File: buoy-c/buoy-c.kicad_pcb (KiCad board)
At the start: 4 copper layers, 49.3 x 87 mm, 102 parts, among them J1 UJ31-CH-G2-SMT-TR, J10 Conn_01x10_Male, J11 TERM-BLK-2P, J12 TERM-BLK-2P, J13 Conn_01x05_Male, J2 BAT-HLD-001-THM, J3 TERM-BLK-2P, J4 U.FL-R-SMT-1_10_, J5 BH-18650-PC, J6 Conn_01x03_Male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

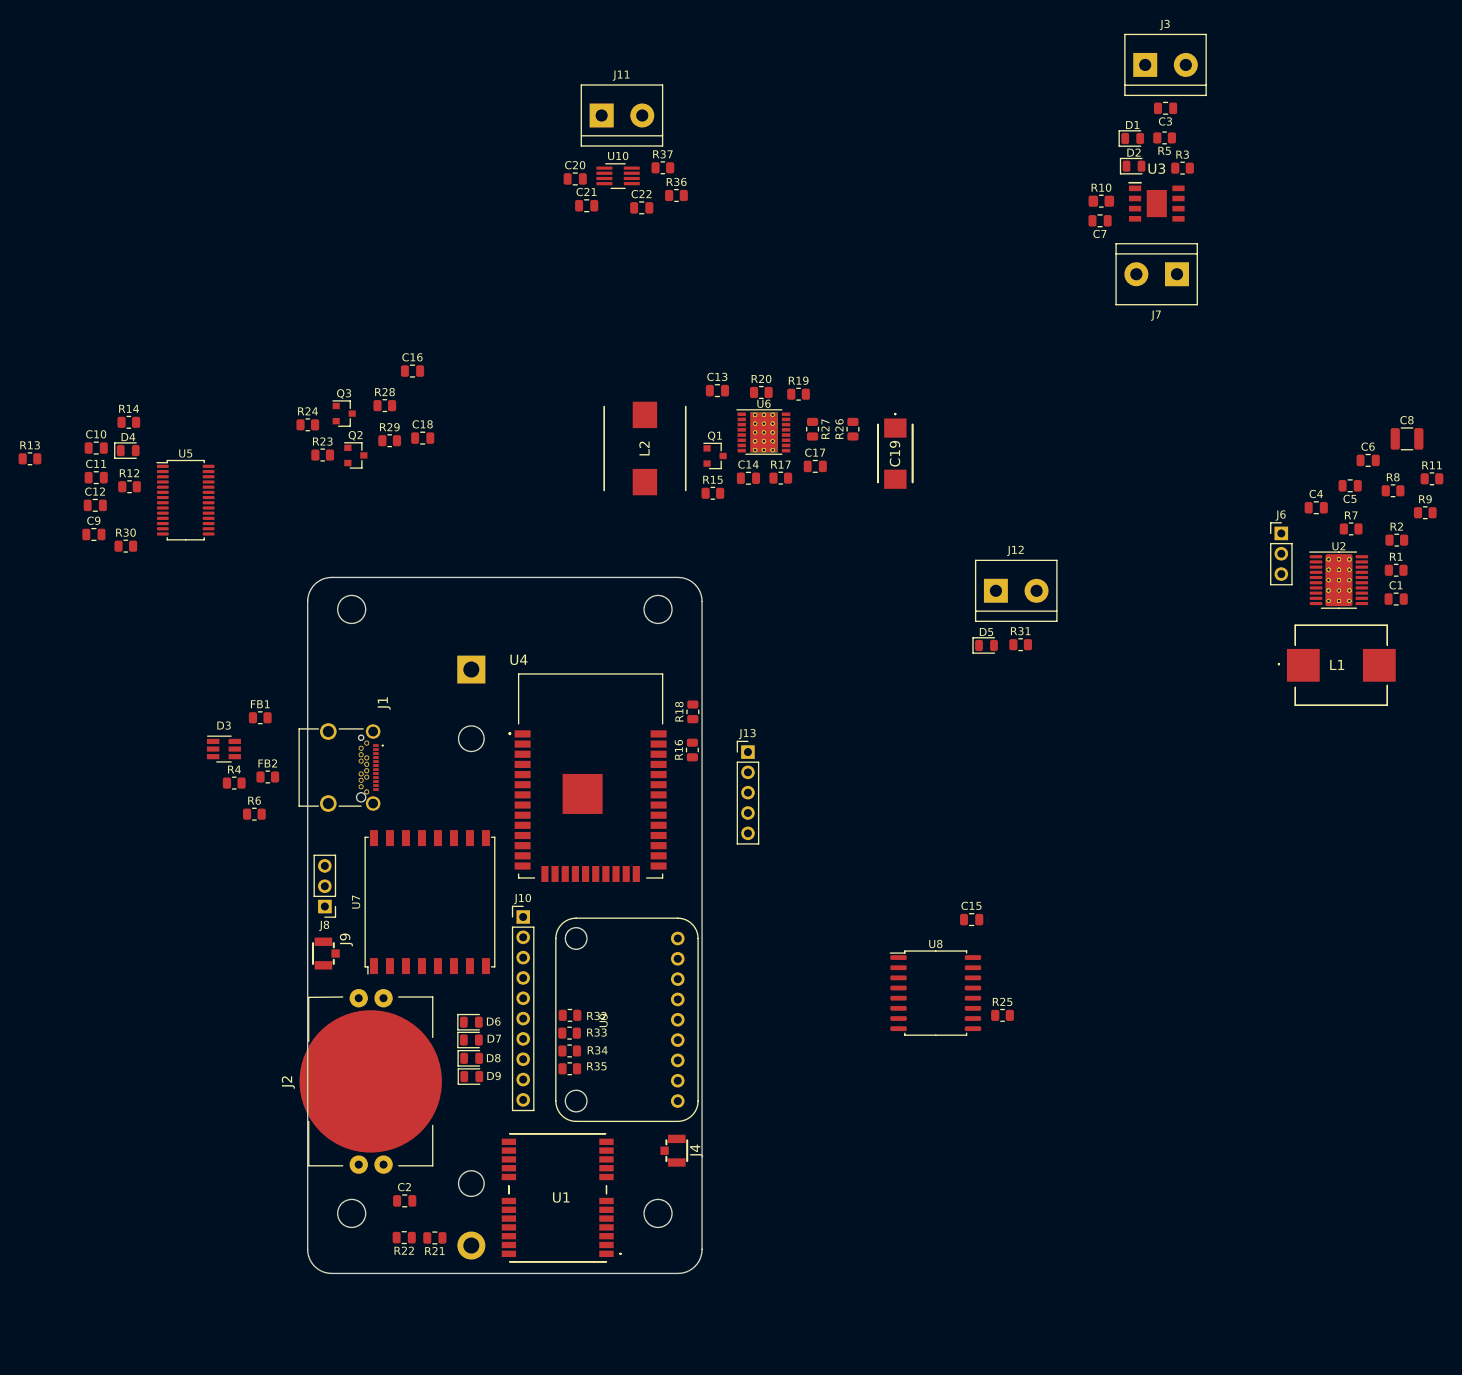
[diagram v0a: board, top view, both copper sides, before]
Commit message: Placed components in the PCB
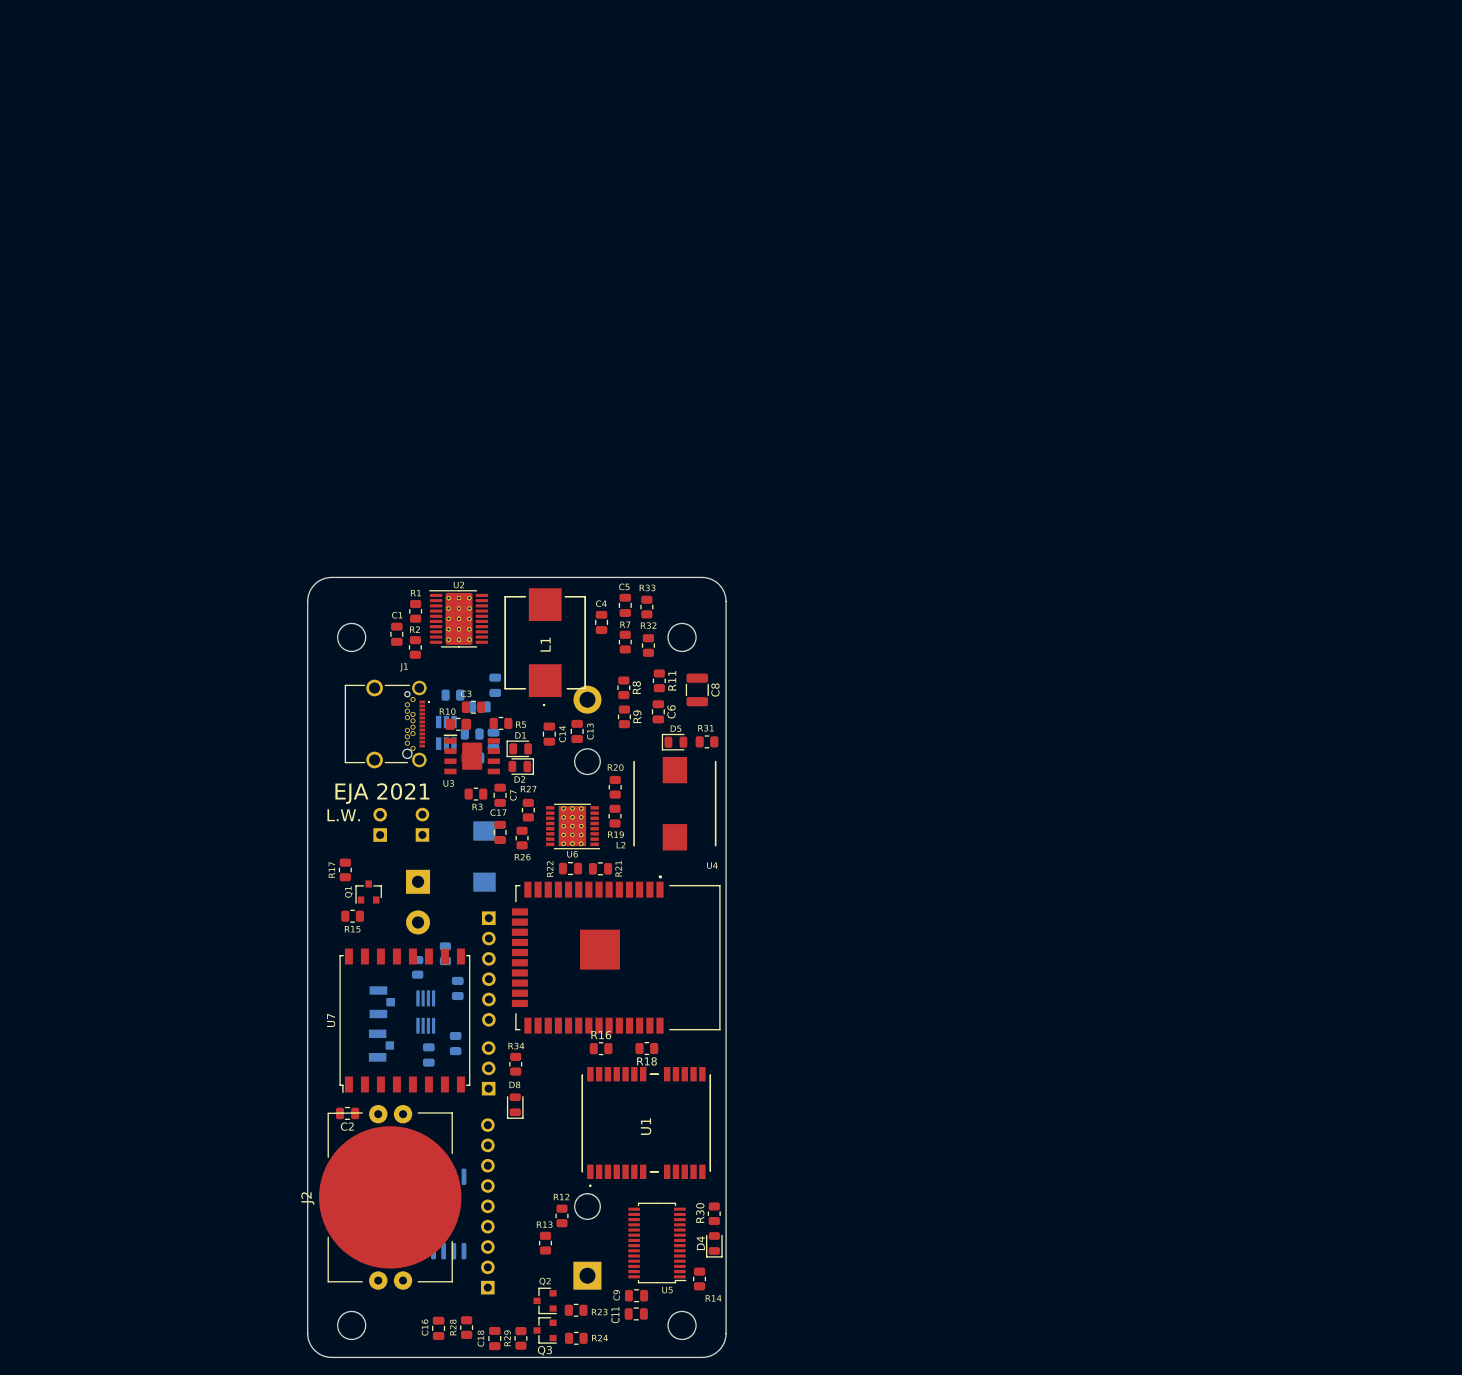
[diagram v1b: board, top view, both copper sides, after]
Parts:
- removed D6: GREEN-CLEAR, LED_SMD:LED_0805_2012Metric
- removed D7: ORANGE-CLEAR, LED_SMD:LED_0805_2012Metric
- removed D9: RED-CLEAR, LED_SMD:LED_0805_2012Metric
- removed J12: TERM-BLK-2P, TerminalBlock:TerminalBlock_bornier-2_P5.08mm
- removed J13: Conn_01x05_Male, Connector_PinHeader_2.54mm:PinHeader_1x05_P2.54mm_Vertical
- removed J6: Conn_01x03_Male, Connector_PinHeader_2.54mm:PinHeader_1x03_P2.54mm_Vertical
- removed R35: 620, Resistor_SMD:R_0805_2012Metric
- removed U9: ADXL343-EVAL, ADXL343-EVAL:ADXL343-EVAL
- added J14: Conn_01x09_Male, Connector_PinHeader_2.54mm:PinHeader_1x09_P2.54mm_Vertical, B.Cu at (122.5, 188.8)
- C10, C12, C15, C19, C20, C21, C22, D3, FB1, FB2, J11, J4, J8, J9, R25, R36, R37, R4, R6, U10, U8: moved to B.Cu
- J10: value Conn_01x10_Male -> Conn_01x06_Male; footprint Connector_PinHeader_2.54mm:PinHeader_1x10_P2.54mm_Vertical -> Connector_PinHeader_2.54mm:PinHeader_1x06_P2.54mm_Vertical; moved to B.Cu
- J3, J7: value TERM-BLK-2P -> Conn_01x02_Male; footprint TerminalBlock:TerminalBlock_bornier-2_P5.08mm -> Connector_PinHeader_2.54mm:PinHeader_1x02_P2.54mm_Vertical; moved to B.Cu
- R32, R33: value 620 -> 0
- moved J3 132.0 mm to (114.3, 132.2)
- moved R14 128.7 mm to (149.0, 187.7), turned to 90 degrees
- moved C1 125.0 mm to (111.1, 107.1), turned to 270 degrees
- moved C11 124.4 mm to (141.1, 192.1)
- moved R2 123.4 mm to (113.5, 108.8), turned to 270 degrees
- moved D4 123.2 mm to (150.8, 183.3), turned to 90 degrees
- moved R1 122.7 mm to (113.5, 104.2), turned to 90 degrees
- moved J7 121.8 mm to (109.1, 132.2), turned to 0 degrees
- moved C16 119.7 mm to (116.4, 193.9), turned to 270 degrees
- moved R24 119.0 mm to (133.6, 195.1)
- moved R3 118.0 mm to (121.0, 127.1)
- moved Q3 117.3 mm to (129.7, 194.1), turned to 180 degrees
- moved R13 117.3 mm to (129.7, 183.2), turned to 90 degrees
- moved C9 116.9 mm to (141.1, 189.8)
- moved R28 115.7 mm to (119.9, 193.8), turned to 90 degrees
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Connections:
- net Net-(D3-Pad3) renamed /FB1
- net Net-(D3-Pad4) renamed /FB2
- J10 pad 2: ESP_IO13 -> ESP_IO6
- J10 pad 3: ESP_IO9 -> ESP_IO7
- J10 pad 4: ESP_IO10 -> ESP_IO8
- J10 pad 5: ESP_IO11 -> ESP_IO15
- J10 pad 6: ESP_IO6 -> ESP_IO2
- R16 pad 1: +BATT -> VDD
- R18 pad 1: +BATT -> VDD
- R32 pad 1: ESP_IO13 -> VDD
- R32 pad 2: Net-(D6-Pad2) -> +3V3
- R33 pad 1: ESP_IO6 -> +BATT
- R33 pad 2: Net-(D7-Pad2) -> VDD
- R34 pad 1: ESP_IO7 -> ESP_IO2
- U4 pad 14: ESP_IO12 -> Net-(U4-Pad14)
- U4 pad 16: ESP_IO13 -> Net-(U4-Pad16)
- U4 pad 17: ESP_IO9 -> Net-(U4-Pad17)
- U4 pad 18: ESP_IO10 -> Net-(U4-Pad18)
- U4 pad 19: ESP_IO11 -> Net-(U4-Pad19)
- U4 pad 4: ESP_IO36 -> Net-(U4-Pad4)
- U4 pad 5: ESP_IO39 -> Net-(U4-Pad5)
- U4 pad 7: ESP_IO35 -> Net-(U4-Pad7)
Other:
- board size 49.3 x 87 mm -> 52.3 x 97.5 mm
- board text added: "+"
- board text added: "-"
- board text added: "5V"
- board text added: "BATT"
- board text added: "EJA 2021"
- board text added: "L.W."
- board text added: "SWITCH"

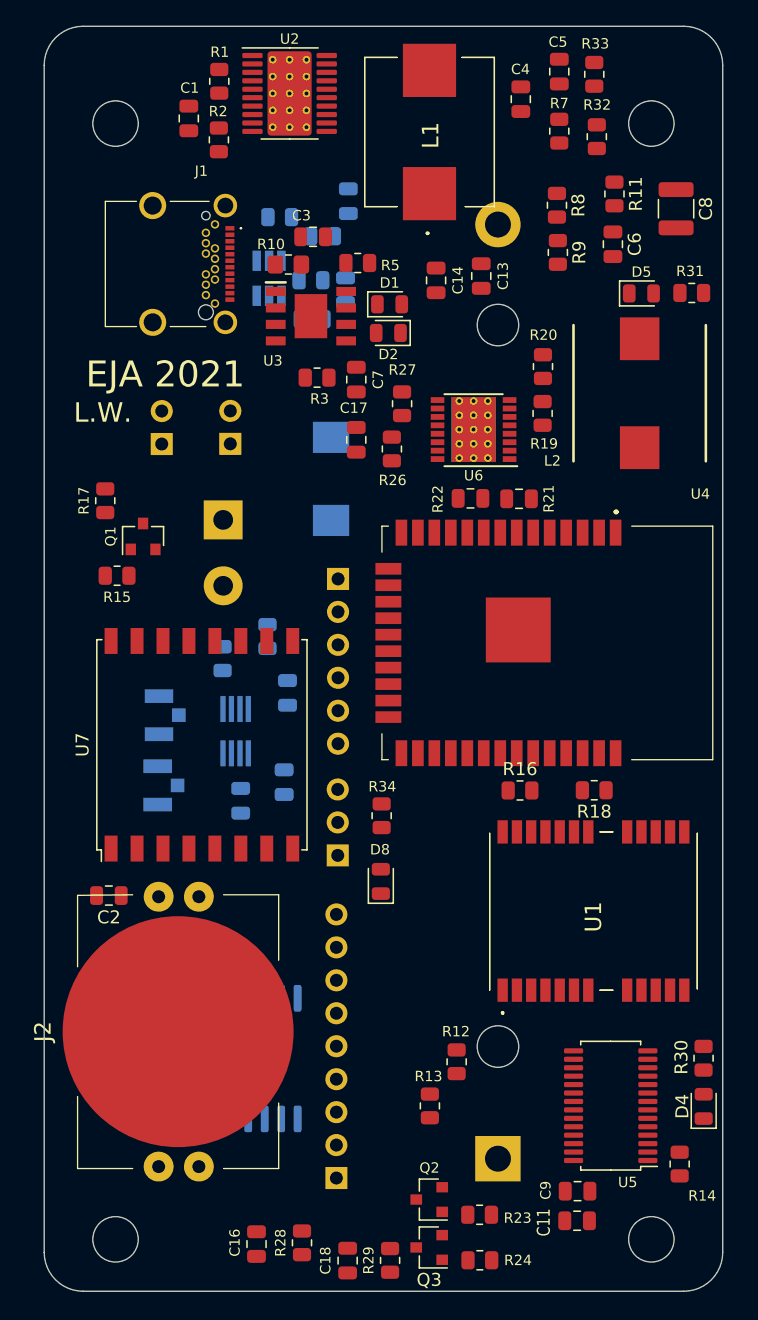
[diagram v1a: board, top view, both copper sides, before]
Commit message: Finished routing, solved unconnected
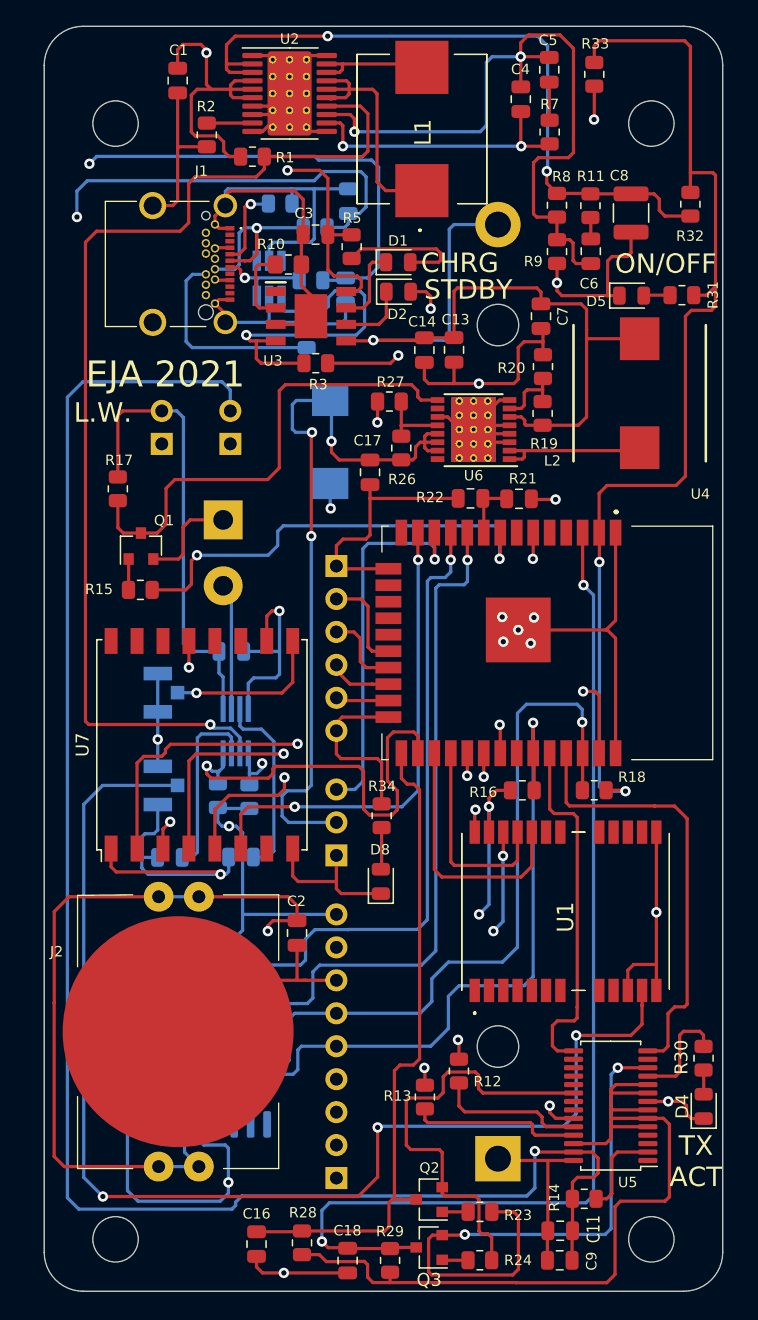
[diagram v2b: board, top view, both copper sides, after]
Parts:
- moved C22 15.6 mm to (109.7, 164.1), turned to 180 degrees
- moved C7 15.1 mm to (138.3, 122.3)
- moved C2 14.8 mm to (119.5, 169.9), turned to 270 degrees
- moved R36 12.4 mm to (115.8, 159.4), turned to 90 degrees
- moved C20 11.5 mm to (114.4, 148.2), turned to 0 degrees
- moved R37 10.6 mm to (113.4, 159.3), turned to 90 degrees
- moved R32 8.89 mm to (149.8, 113.7), turned to 270 degrees
- moved R14 7.83 mm to (141.6, 190.4), turned to 0 degrees
- moved C21 6.66 mm to (115.2, 164.0), turned to 180 degrees
- moved R1 6.34 mm to (116.1, 110.0), turned to 0 degrees
- moved C13 6.07 mm to (131.6, 124.9)
- moved C9 5.51 mm to (139.7, 195.1), turned to 180 degrees
- moved C14 5.45 mm to (129.3, 125.0)
- moved C8 3.49 mm to (145.2, 114.4)
- moved D1 3.31 mm to (127.3, 118.2)
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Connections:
- J8 pad 2: PWM_SERVO -> +5V
- J8 pad 3: +5V -> PWM_SERVO
- U3 pad 9: (no net) -> GND
- U7 pad 3: LORA_MISO -> LORA_MOSI
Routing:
- net GND: track 0.00 -> 351.1 mm, vias 0 -> 18
- net +BATT: track 0.00 -> 232.6 mm, vias 0 -> 4
- net /5V_USB: track 0.00 -> 208.6 mm, vias 0 -> 3
- net VDD: track 0.00 -> 183.5 mm, vias 0 -> 6
- net /D-: track 0.00 -> 131.3 mm, vias 0 -> 2
- net /D+: track 0.00 -> 124.1 mm, vias 0 -> 2
- net Net-(J4-Pad3): track 0.00 -> 94.1 mm, vias 0 -> 3
- net LORA_MOSI: track 0.00 -> 83.9 mm, vias 0 -> 2
- net EN_3V3: track 0.00 -> 83.9 mm, vias 0 -> 1
- net BAT-CR2032: track 0.00 -> 83.0 mm, vias 0 -> 3
- net ESP_EN: track 0.00 -> 82.8 mm, vias 0 -> 2
- net SCL: track 0.00 -> 68.8 mm, vias 0 -> 1
- net 3V3_FTDI: track 0.00 -> 65.1 mm
- net SDA: track 0.00 -> 62.0 mm, vias 0 -> 1
- net RST_RTC: track 0.00 -> 59.4 mm, vias 0 -> 1
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- added copper zone on GND.Cu, net GND
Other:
- board text added: "5V USB"
- board text added: "ACC"
- board text added: "AUX"
- board text added: "CHRG"
- board text added: "GND"
- board text added: "GPS"
- board text added: "IO15"
- board text added: "IO2"
- board text added: "IO6"
- board text added: "IO7"
- board text added: "IO8"
- board text added: "LoRa"
- board text added: "ON/OFF"
- board text added: "PWM"
- board text added: "SCL"
- board text added: "SDA"
- board text added: "SERVO"
- board text added: "STDBY"
- board text added: "TX ACT"
- board text added: "VDD"
